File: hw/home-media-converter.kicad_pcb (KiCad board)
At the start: 4 copper layers, 79.6 x 54 mm, 148 parts, among them J2 Conn_01x04_Male, J3 Conn_01x03, J4 Conn_01x03, J5 Conn_01x03, J6 RJ45_LED_Shielded, J7 USB_B, SW1 SW_Push, U1 KSZ9131RNXC-TR, U2 STM32F030F4Px, U3 DP83TG720RWRHATQ1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

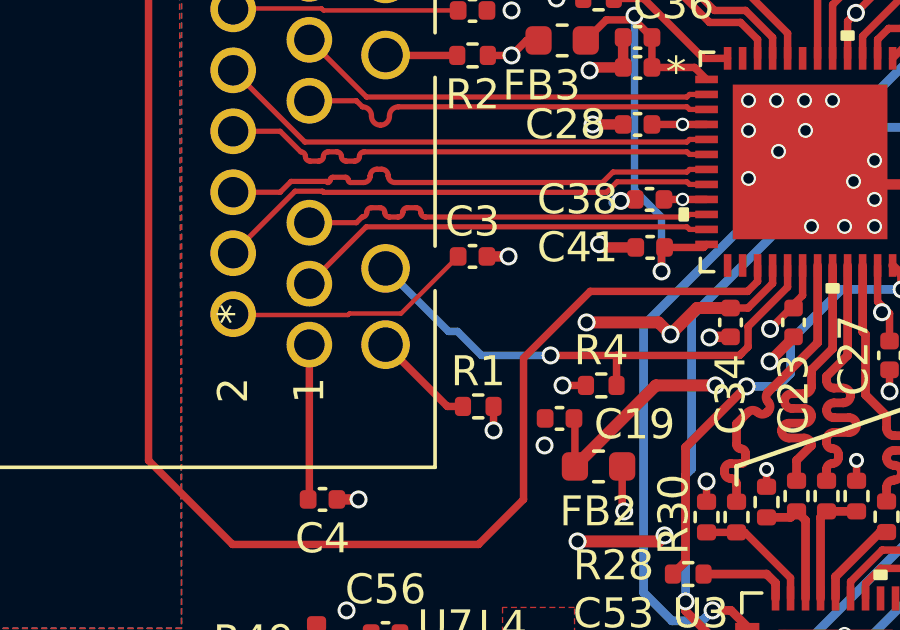
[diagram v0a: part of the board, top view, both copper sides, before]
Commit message: Fix MagJack LED polarity
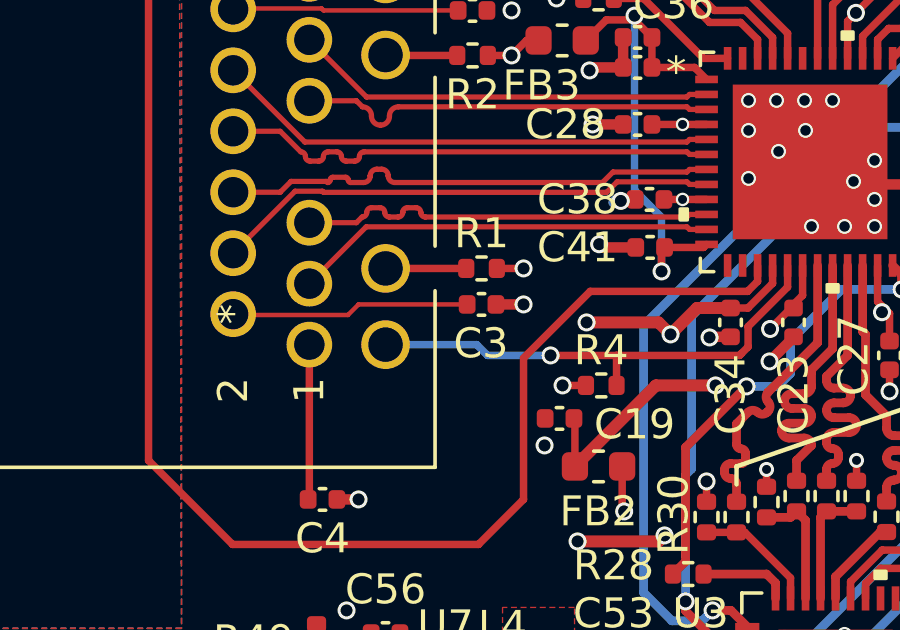
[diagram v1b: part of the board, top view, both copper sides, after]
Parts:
- C14, C15, C6, C7: value C -> 26p
- FB2, FB3: value FerriteBead -> BLM18PG121SN1D
- FB4, FB6: value FerriteBead -> BLM18KG601SH1
- FB5: value FerriteBead -> BLM18HE102SN1
- moved R1 4.60 mm to (68.0, 124.0)
- moved C3 1.63 mm to (68.0, 125.2)
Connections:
- R1 pad 1: Net-(J1-LED_YEL_N) -> Net-(J1-LED_YEL_P)
- R4 pad 2: Net-(J1-LED_YEL_P) -> Net-(J1-LED_YEL_N)
- U1 pad 17: Net-(J1-LED_YEL_P) -> Net-(J1-LED_YEL_N)
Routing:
- net Net-(J1-LED_YEL_P): track 17.7 -> 2.69 mm, vias 1 -> 0
- net Net-(J1-LED_YEL_N): track 3.43 -> 16.6 mm, vias 0 -> 1
